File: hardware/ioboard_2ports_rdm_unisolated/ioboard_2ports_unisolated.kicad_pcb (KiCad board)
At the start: 2 copper layers, 106 x 55 mm, 27 parts, among them J1 Conn_02x06_Odd_Even, J12 Conn_01x03, J2 XLR3, J3 XLR3, J6 Conn_01x03, J8 XLR3, J9 XLR3, U1 M24C02-WMN, U2 SP3485EN, U3 XC6206PxxxMR, U4 SP3485EN

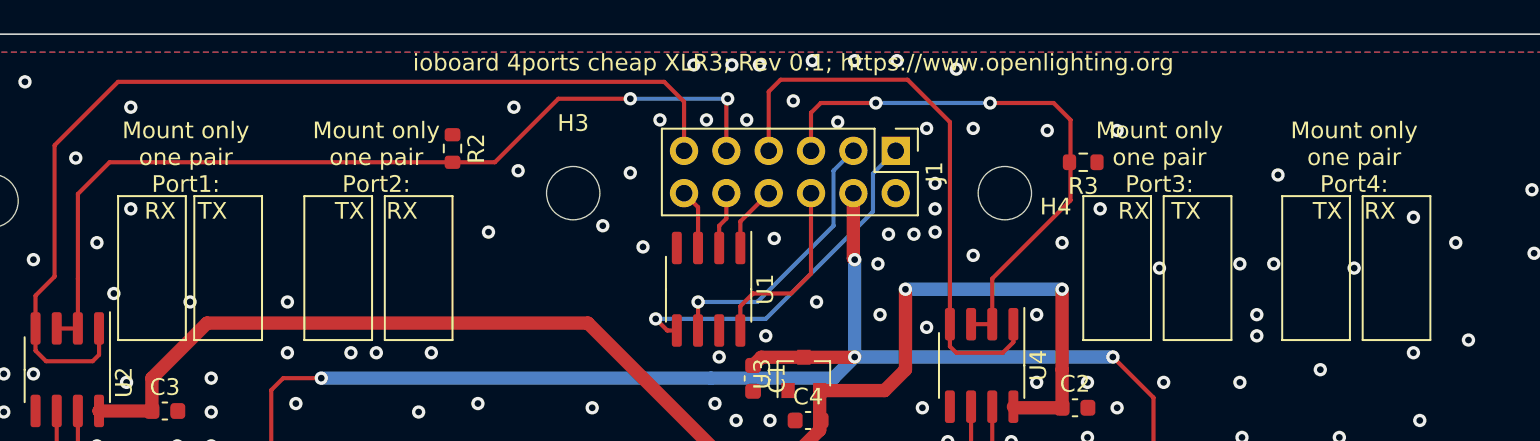
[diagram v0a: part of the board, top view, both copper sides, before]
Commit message: Unify board naming and bump all to rev 0.2
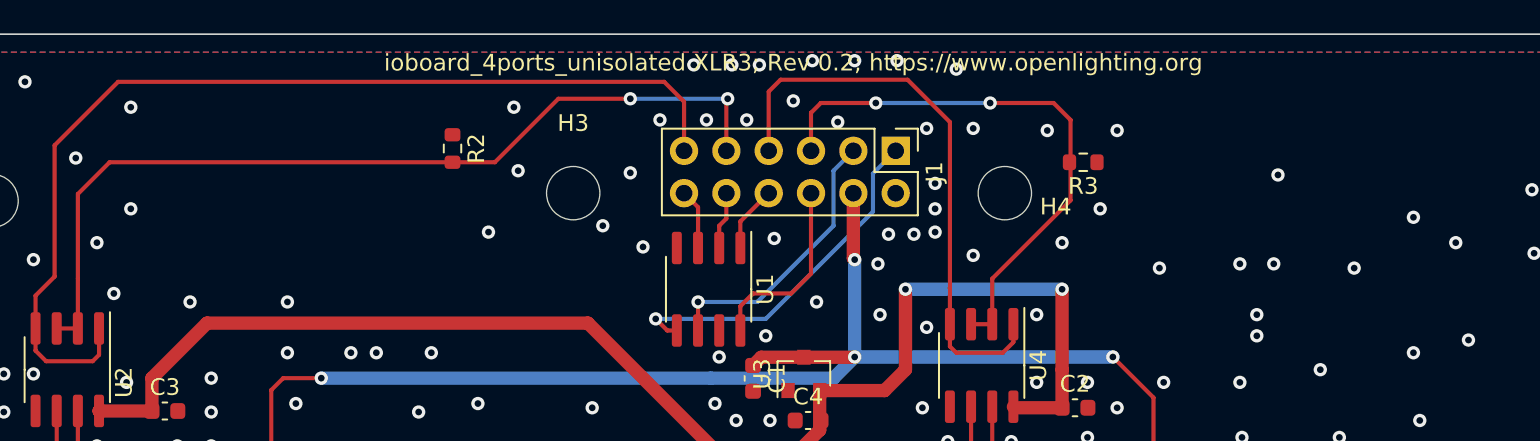
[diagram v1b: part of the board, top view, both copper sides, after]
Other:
- board text added: "ioboard_4ports_unisolated XLR3; Rev 0.2; https://www.openlighting.org"
- board text removed: "Mount only one pair Port1: RX TX"
- board text removed: "Mount only one pair Port2: TX RX"
- board text removed: "Mount only one pair Port3: RX TX"
- board text removed: "Mount only one pair Port4: TX RX"
- board text removed: "ioboard 4ports cheap XLR3; Rev 0.1; https://www.openlighting.org"

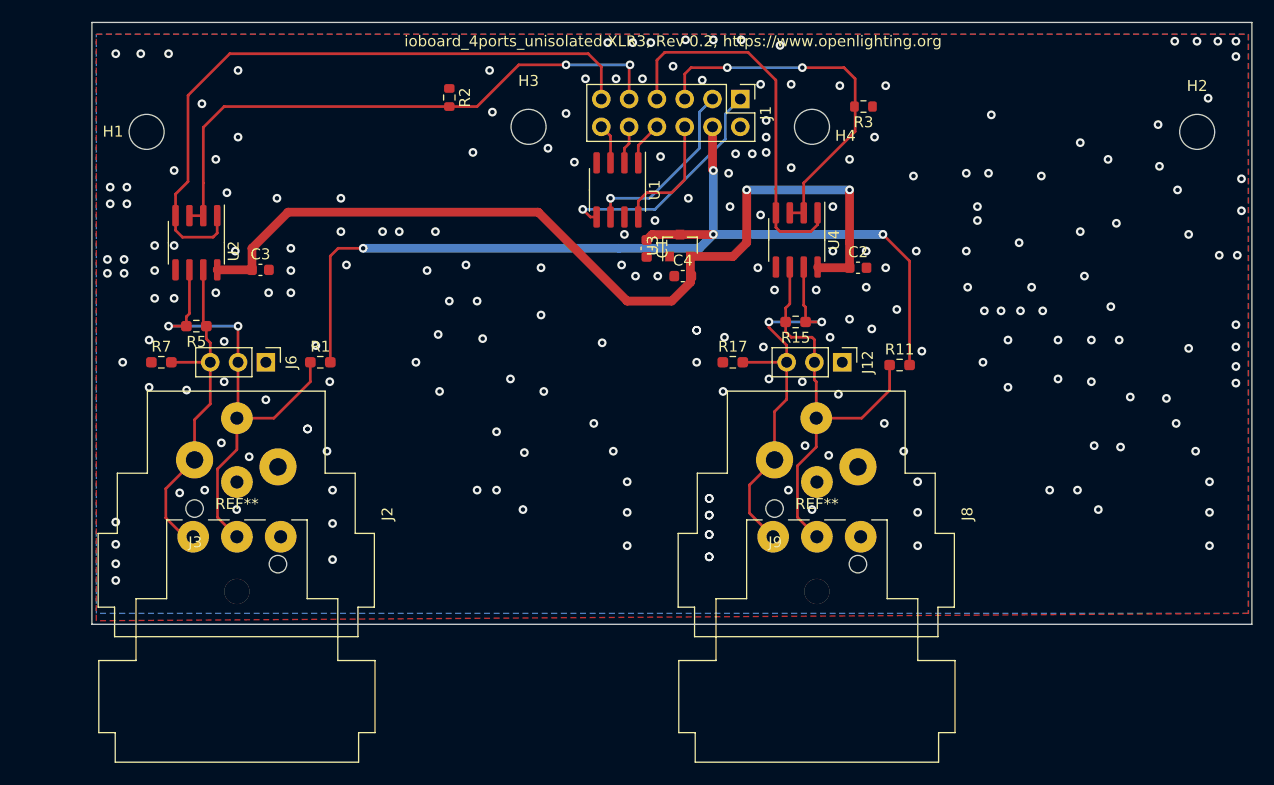
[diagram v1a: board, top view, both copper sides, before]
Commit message: ioboard_2ports_rdm_unisolated: Use AMS1117 LDO instead of the more exotic XC6206. Bump to Rev 0.3
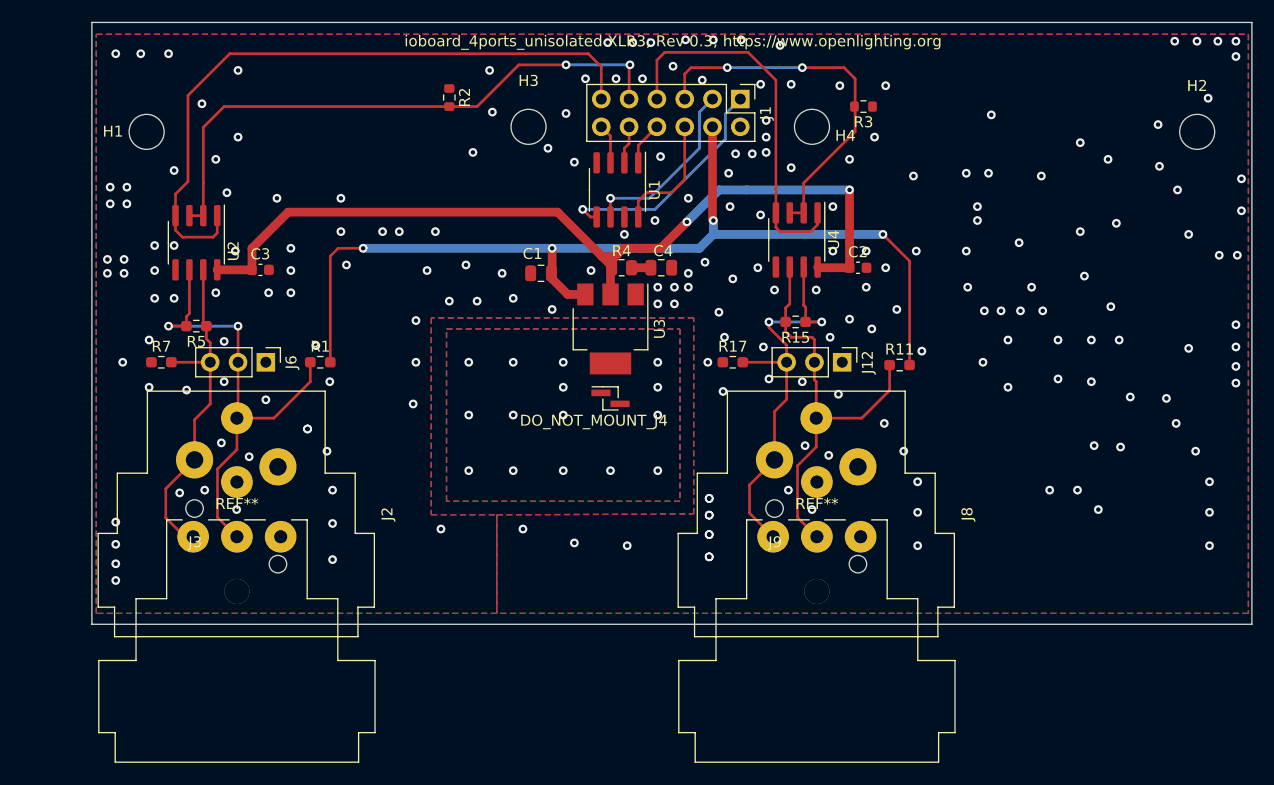
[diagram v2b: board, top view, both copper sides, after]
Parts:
- added DO_NOT_MOUNT_J4: Conn_01x01_DO_NOT_MOUNT, Connector_PinHeader_1.00mm:PinHeader_1x02_P1.00mm_Vertical_SMD_Pin1Left, F.Cu at (72.4, 54.4)
- added R4: 1R, Resistor_SMD:R_0805_2012Metric, F.Cu at (73.4, 42.4)
- C1, C4: value 1uF -> 22uF; footprint Capacitor_SMD:C_0603_1608Metric -> Capacitor_SMD:C_0805_2012Metric
- U3: value XC6206PxxxMR -> AMS1117-3.3; footprint Package_TO_SOT_SMD:SOT-23 -> Package_TO_SOT_SMD:SOT-223
- moved U3 9.92 mm to (72.4, 48.0), turned to 270 degrees
- moved C1 9.92 mm to (66.0, 42.9), turned to 180 degrees
- moved C4 2.11 mm to (77.0, 42.4), turned to 180 degrees
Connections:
- C4 pad 2: /+3V3_INT -> Net-(C4-Pad2)
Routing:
- net /+3V3_INT: track 83.0 -> 80.3 mm
- net Net-(C4-Pad2): track 0.00 -> 1.76 mm
- net Net-(DO_NOT_MOUNT_J4-Pad1): vias 0 -> 15
- net GND: vias 222 -> 218
- added copper zone on B.Cu, net Net-(DO_NOT_MOUNT_J4-Pad1)
- added copper zone on F.Cu, net Net-(DO_NOT_MOUNT_J4-Pad1)
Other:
- board text added: "ioboard_4ports_unisolated XLR3; Rev 0.3; https://www.openlighting.org"
- board text removed: "ioboard_4ports_unisolated XLR3; Rev 0.2; https://www.openlighting.org"

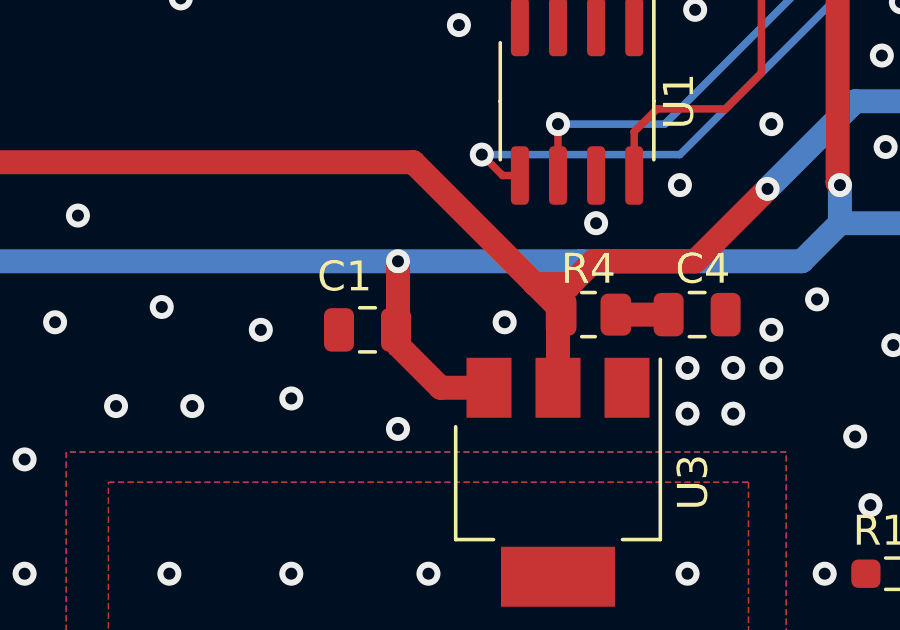
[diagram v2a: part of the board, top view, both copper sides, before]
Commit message: Refine placement of one capacitor
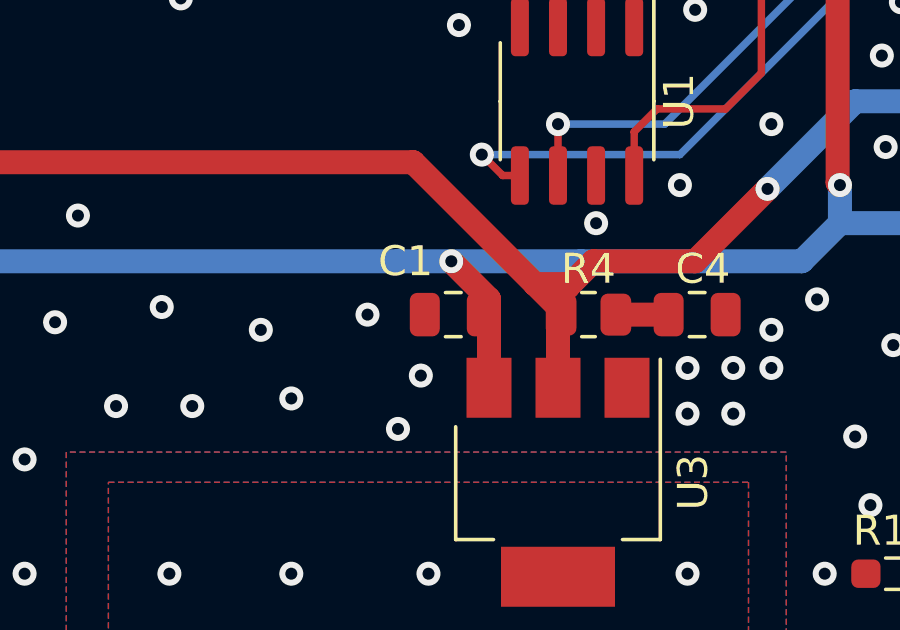
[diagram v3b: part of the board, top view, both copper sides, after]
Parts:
- moved C1 2.90 mm to (68.9, 42.4)
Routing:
- net +5V: track 90.2 -> 88.6 mm
- net GND: vias 218 -> 219

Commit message: Hardware: Make the reference path to the library relative and save the files with the new kicad version
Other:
- net class Default removed

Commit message: Finish IO-Board updates
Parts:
- DO_NOT_MOUNT_J4: footprint Connector_PinHeader_1.00mm:PinHeader_1x02_P1.00mm_Vertical_SMD_Pin1Left -> TestPoint:TestPoint_Pad_D4.0mm
- U1: value M24C02-WMN -> M24C64-RMN6TP
- moved DO_NOT_MOUNT_J4 2.95 mm to (70.9, 56.9)
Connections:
- DO_NOT_MOUNT_J4 pad 1: Net-(DO_NOT_MOUNT_J4-Pad1) -> unconnected-(DO_NOT_MOUNT_J4-Pad1)
- U3 pad 4: Net-(DO_NOT_MOUNT_J4-Pad1) -> unconnected-(DO_NOT_MOUNT_J4-Pad1)
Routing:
- net unconnected-(DO_NOT_MOUNT_J4-Pad1): vias 0 -> 15
- net Net-(DO_NOT_MOUNT_J4-Pad1): vias 15 -> 0
- net GND: vias 219 -> 214
- added copper zone on B.Cu, net unconnected-(DO_NOT_MOUNT_J4-Pad1)
- added copper zone on F.Cu, net unconnected-(DO_NOT_MOUNT_J4-Pad1)
- removed copper zone on B.Cu, net Net-(DO_NOT_MOUNT_J4-Pad1)
- removed copper zone on F.Cu, net Net-(DO_NOT_MOUNT_J4-Pad1)
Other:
- board text added: "ioboard_4ports_unisolated XLR3; Rev 0.5; https://github.com/OpenLightingProject/rp2040-dmxsun"
- board text removed: "ioboard_4ports_unisolated XLR3; Rev 0.3; https://www.openlighting.org"

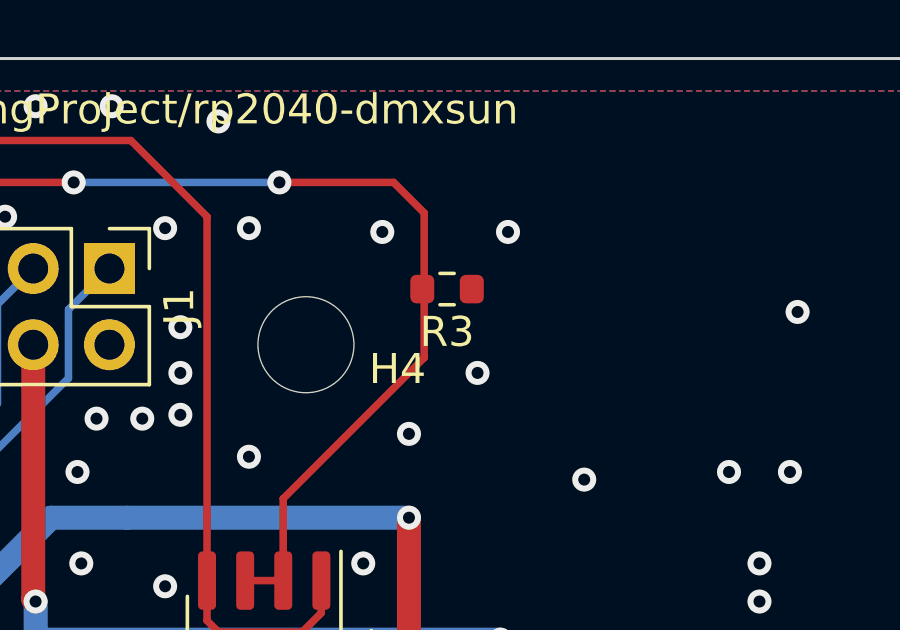
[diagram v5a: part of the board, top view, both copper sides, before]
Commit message: Ignore some more ERC and DRC errors
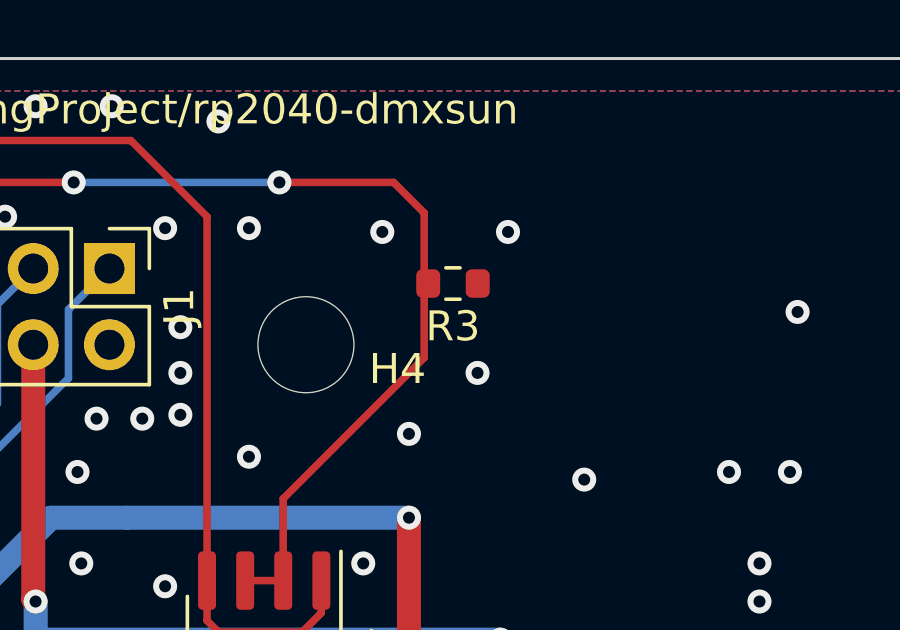
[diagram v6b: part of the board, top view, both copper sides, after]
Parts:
- moved R3 0.27 mm to (95.7, 27.5)
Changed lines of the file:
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@@
   )
   (footprint "Resistor_SMD:R_0603_1608Metric" (layer "F.Cu")
-    (at 95.504 27.686 180)
+    (at 95.7 27.5 180)
     (descr "Resistor SMD 0603 (1608 Metric), square (rectangular) end terminal, IPC_7351 nominal, (Body size source: IPC-SM-782 page 72, https://www.pcb-3d.com/wordpress/wp-content/uploads/ipc-sm-782a_amendment_1_and_2.pdf), generated with kicad-footprint-generator")
     (tags "resistor")
@@
     (pts (xy 25 75) (xy 25 20))
     (height -3.918)
-    (gr_text "55,0000 mm" (at 19.932 47.5 90) (layer "Dwgs.User")
+    (gr_text "55.0000 mm" (at 19.932 47.5 90) (layer "Dwgs.User")
       (effects (font (size 1 1) (thickness 0.15)))
     )
@@
       013e0677-439e-4c5c-81ed-d0f42e2fd361
       024315db-f1ab-42d3-b6eb-ddcfd6322368
-      02bcfffb-06e2-4398-b6ea-84554c2ee3cf
       04fd24e7-8642-4ec7-979c-58477de2d536
       05ae880a-5f6c-4a7c-8655-cbf401c1fe8b
@@
       367c2a5e-c4ef-436d-adda-2c6450a2663e
       3775be67-55eb-4b13-a266-430db87c832b
-      3b6f9837-7ea9-413e-94e0-3e88d9674ae2
       3c1a1dc5-505c-4e36-9830-87ca8e1c359a
       3c9aeeb5-e225-40b7-a206-cadc6e8c5ef5
@@
       a4405d08-5b09-451a-b5c3-d293dfc26ac9
       a4f197d3-f95a-4223-b489-0274d5e96e47
-      a5e251fd-7096-4699-bd41-fe475dc7e156
       a5f618ac-f871-44b8-beed-2cb541f72022
       a613377c-5634-4662-9878-cdedacbd2bc4
@@
       a69eb000-1e89-47ea-8d8f-ebdda33c68de
       a6dfd677-396d-4178-ac3a-6a8b007a2eaa
-      a7d9977f-99c4-4a93-9956-d93039a173f6
       a7f498db-c614-40cb-ac59-d1099e0679de
       a80d346b-57f2-42e6-a793-fbf7cd2595d7
@@
       dc24d890-f0e4-4bbe-86a7-94b2b77a1648
       dc82dbf3-b356-4a1c-afa2-ad291e3ebbf9
-      dca6c863-1b06-4de1-b05d-0a4dc05f47f5
       ddde503c-feee-46b9-9354-ef64f426001b
       ddf0137b-6454-4918-a57e-16d96dd8ad43
@@
       e48b715b-3636-4c32-af94-17d9ed22dbea
       e48d95c2-d38f-479a-814f-84146a4f23e8
-      e712cb6c-ce46-48a5-827c-4e43dafc65b7
-      e83c1611-ae7e-4cfa-9991-060b2625eb9e
       e868140d-5094-4877-88c2-623f0fe852f5
       e974a797-cc6a-4ac1-9083-23a4c0d9933d

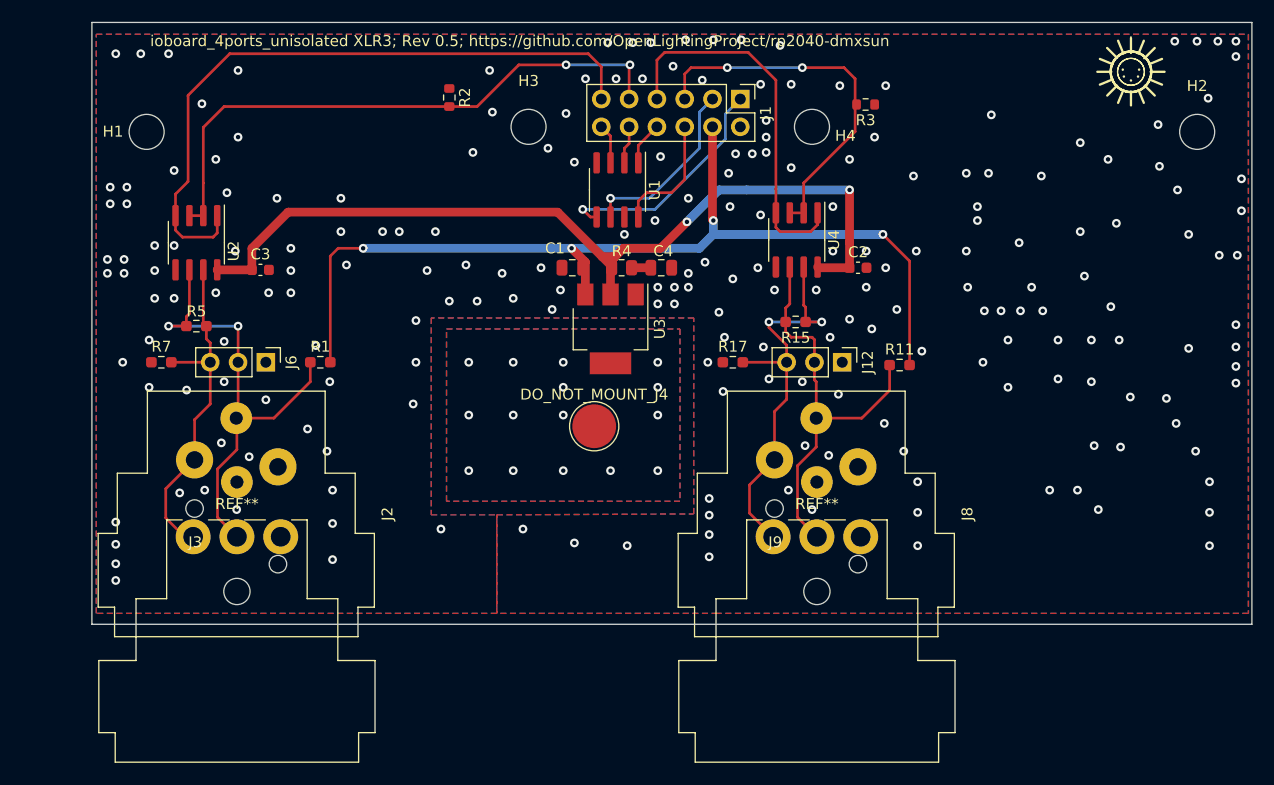
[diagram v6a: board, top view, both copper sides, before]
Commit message: Add RJ45 jacks to ioboard_2ports_rdm_unisolated as well
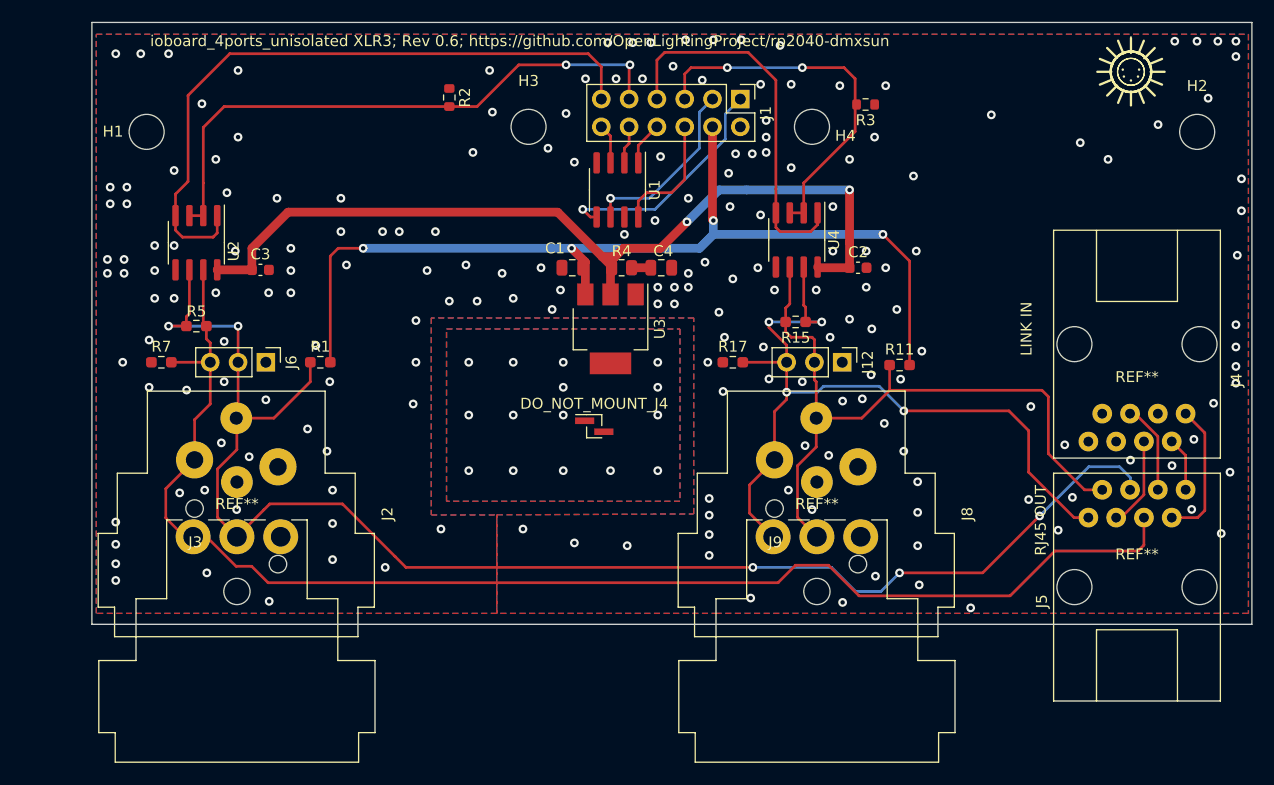
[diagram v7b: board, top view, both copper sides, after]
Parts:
- added J4: 8P8C, RJ45_Sparkfun:RJ45_Sparkfun, F.Cu at (120.5, 49.4)
- added J5: 8P8C, RJ45_Sparkfun:RJ45_Sparkfun, F.Cu at (120.5, 71.6)
- DO_NOT_MOUNT_J4: footprint TestPoint:TestPoint_Pad_D4.0mm -> Connector_PinHeader_1.00mm:PinHeader_1x02_P1.00mm_Vertical_SMD_Pin1Left
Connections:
- net Net-(J12-Pad2) renamed /RJ45_OUT_4
- net Net-(J12-Pad3) renamed /RJ45_OUT_3
- net Net-(J2-Pad2) renamed /RJ45_OUT_2
- net Net-(J2-Pad3) renamed /RJ45_OUT_1
- U3 pad 4: unconnected-(DO_NOT_MOUNT_J4-Pad1) -> (no net)
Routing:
- net /RJ45_OUT_2: track 31.4 -> 126.3 mm
- net /RJ45_OUT_1: track 43.9 -> 136.3 mm, vias 2 -> 5
- net /RJ45_OUT_3: track 38.0 -> 73.0 mm, vias 2 -> 4
- net /RJ45_OUT_4: track 38.6 -> 64.8 mm
- net /RJ45_LINK_3: track 0.00 -> 12.9 mm
- net /RJ45_LINK_1: track 0.00 -> 8.28 mm
- net /RJ45_LINK_2: track 0.00 -> 8.27 mm
- net /RJ45_LINK_4: track 0.00 -> 4.94 mm
- net GND: vias 214 -> 195
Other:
- board text added: "LINK IN"
- board text added: "RJ45 OUT"
- board text added: "ioboard_4ports_unisolated XLR3; Rev 0.6; https://github.com/OpenLightingProject/rp2040-dmxsun"
- board text removed: "ioboard_4ports_unisolated XLR3; Rev 0.5; https://github.com/OpenLightingProject/rp2040-dmxsun"
